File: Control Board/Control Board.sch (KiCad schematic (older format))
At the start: 77 parts, among them J1 Conn_02x03_Odd_Even, J2 Conn_02x25_Counter_Clockwise, Q1 STS4DNF60L, SW1 SW_SPDT, U1 ATXMEGA128A3-AU, U2 LT1797, U3 LT1797, U4 ISL83490, U5 MAX31856, U6 MAX31856, U7 MAX31856, U8 MAX31856, U9 MAX31856

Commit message: Updated power board to kicad 5
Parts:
- C1, C10, C11, C12, C13, C14, C15, C16, C17, C18, C19, C2, C20, C21, C22, C23, C24, C25, C26, C27, C28, C29, C3, C30, C31, C32, C33, C34, C35, C4, C5, C6, C7, C8, C9: symbol C_Small -> device:C_Small
- D1, D2, D3, D4: symbol LED -> device:LED
- J1: symbol Conn_02x03_Odd_Even -> Control-Board-rescue:Conn_02x03_Odd_Even
- J2: symbol Conn_02x25_Counter_Clockwise -> Control-Board-rescue:Conn_02x25_Counter_Clockwise
- L1: symbol L_Small -> device:L_Small
- Q1: symbol STS4DNF60L -> Custom-Parts:STS4DNF60L
- R1, R10, R11, R12, R13, R14, R15, R16, R17, R18, R19, R2, R20, R21, R3, R4, R5: symbol R_Small -> device:R_Small
- R22, R6, R7, R8, R9: symbol R -> device:R
- RN1, RN2: symbol Voltage_Divider_CenterPin3 -> device:Voltage_Divider_CenterPin3
- SW1: symbol SW_SPDT -> Control-Board-rescue:SW_SPDT
- U1: symbol ATXMEGA128A3-AU -> atmel:ATXMEGA128A3-AU
- U2, U3: symbol LT1797 -> Custom-Parts:LT1797
- U4: symbol ISL83490 -> Custom-Parts:ISL83490
- U5, U6, U7, U8, U9: symbol MAX31856 -> Custom-Parts:MAX31856
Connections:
- wire segments 235 -> 292

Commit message: Forgot an openlog on the control board
Had to get rid of the fault detect pins on the TCs, will have to poll for faults over SPI now
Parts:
- added U?: OPENLOG, symbol Custom-Parts:OPENLOG
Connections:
- net labels added: OPENLOG_RX, OPENLOG_TX
- net labels removed: BUZZER1, BUZZER2, TC1_FAULT, TC2_FAULT, TC3_FAULT, TC4_FAULT, TC5_FAULT
- wire segments 292 -> 288
- no-connect marks 0 -> 1

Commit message: A whole lot of changes
Kinda forgot what they all were
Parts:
- removed J2: Conn_02x25_Counter_Clockwise, Custom Footprints:CONN_CARD_02x25_MALE, symbol Control-Board-rescue:Conn_02x25_Counter_Clockwise
- removed R1, R2: 1.8 kΩ, Resistors_SMD:R_0603, symbol device:R_Small
- added J1: Conn_02x10_Odd_Even, symbol Connector:Conn_02x10_Odd_Even
- added J?: RJ45, Connectors:RJ45_8, symbol Connector:RJ45
- added J? (x4): GS3, Connectors:GS3, symbol Connector:GS3
- added J?: Conn_01x10, Connectors_JST:JST_PH_S10B-PH-K_10x2.00mm_Angled, symbol Connector:Conn_01x10
- renumbered J1 to J2
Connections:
- net labels removed: +14V
- wire segments 288 -> 305
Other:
- note removed: "Close to power supply"
- note removed: "TODO: Figure out how to control the servos\nThis assumes its 5V PWM, change this if it's not"
- moved on the sheet: R3, R4

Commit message: Starting to make control board match power board
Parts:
- removed J? (x4): GS3, Connectors:GS3, symbol Connector:GS3
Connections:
- wire segments 305 -> 285
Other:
- note added: "Needs crossover cable"
- moved on the sheet: J?
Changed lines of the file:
@@
 L power:+3V3 #PWR075
 U 1 1 5A835285
-P 13800 11300
-F 0 "#PWR075" H 13800 11150 50  0001 C CNN
-F 1 "+3V3" V 13800 11500 50  0000 C CNN
-F 2 "" H 13800 11300 50  0001 C CNN
-F 3 "" H 13800 11300 50  0001 C CNN
-	1    13800 11300
+P 14350 10750
+F 0 "#PWR075" H 14350 10600 50  0001 C CNN
+F 1 "+3V3" V 14350 10950 50  0000 C CNN
+F 2 "" H 14350 10750 50  0001 C CNN
+F 3 "" H 14350 10750 50  0001 C CNN
+	1    14350 10750
 	0    -1   -1   0
 $EndComp
@@
 Text Label 2150 4600 2    60   ~ 0
 BOARD_TX
-Text Label 12600 13100 3    60   ~ 0
+Text Label 12000 12650 3    60   ~ 0
 BOARD_RX+
-Text Label 11800 13100 3    60   ~ 0
+Text Label 11800 12650 3    60   ~ 0
 BOARD_TX+
-Text Label 13000 13100 3    60   ~ 0
+Text Label 12300 12650 3    60   ~ 0
 BOARD_RX-
-Text Label 12200 13100 3    60   ~ 0
+Text Label 11900 12650 3    60   ~ 0
 BOARD_TX-
 Text Label 8450 12250 2    60   ~ 0
@@
 L power:GND #PWR092
 U 1 1 5A9DF128
-P 13700 11900
-F 0 "#PWR092" H 13700 11650 50  0001 C CNN
-F 1 "GND" V 13700 11700 50  0000 C CNN
-F 2 "" H 13700 11900 50  0001 C CNN
-F 3 "" H 13700 11900 50  0001 C CNN
-	1    13700 11900
-	0    -1   1    0
+P 14350 10850
+F 0 "#PWR092" H 14350 10600 50  0001 C CNN
+F 1 "GND" V 14350 10650 50  0000 C CNN
+F 2 "" H 14350 10850 50  0001 C CNN
+F 3 "" H 14350 10850 50  0001 C CNN
+	1    14350 10850
+	0    1    -1   0
 $EndComp
 Text Label 14350 12250 2    60   ~ 0
@@
 L power:GND #PWR?
 U 1 1 5AB3D167
-P 12700 11500
-F 0 "#PWR?" H 12700 11250 50  0001 C CNN
-F 1 "GND" V 12700 11300 50  0000 C CNN
-F 2 "" H 12700 11500 50  0001 C CNN
-F 3 "" H 12700 11500 50  0001 C CNN
-	1    12700 11500
+P 12700 11850
+F 0 "#PWR?" H 12700 11600 50  0001 C CNN
+F 1 "GND" V 12700 11650 50  0000 C CNN
+F 2 "" H 12700 11850 50  0001 C CNN
+F 3 "" H 12700 11850 50  0001 C CNN
+	1    12700 11850
 	0    -1   1    0
 $EndComp
@@
 L Connector:RJ45 J?
 U 1 1 5ADD31C9
-P 12150 11850
-F 0 "J?" H 12226 12467 50  0000 C CNN
-F 1 "RJ45" H 12226 12376 50  0000 C CNN
-F 2 "Connectors:RJ45_8" H 12150 11850 50  0001 C CNN
-F 3 "" H 12150 11850 50  0001 C CNN
-	1    12150 11850
+P 12150 12200
+F 0 "J?" H 12226 12817 50  0000 C CNN
+F 1 "RJ45" H 12226 12726 50  0000 C CNN
+F 2 "Connectors:RJ45_8" H 12150 12200 50  0001 C CNN
+F 3 "" H 12150 12200 50  0001 C CNN
+	1    12150 12200
 	1    0    0    -1
 $EndComp
-$Comp
-L Connector:GS3 J?
-U 1 1 5AE56887
-P 11800 12950
-F 0 "J?" V 11754 13118 50  0000 L CNN
-F 1 "GS3" V 11845 13118 50  0000 L CNN
-F 2 "Connectors:GS3" V 11888 12876 50  0001 C CNN
-F 3 "" H 11800 12950 50  0001 C CNN
-	1    11800 12950
-	0    1    1    0
-$EndComp
-$Comp
-L Connector:GS3 J?
-U 1 1 5AE74912
-P 12200 12950
-F 0 "J?" V 12154 13118 50  0000 L CNN
-F 1 "GS3" V 12245 13118 50  0000 L CNN
-F 2 "Connectors:GS3" V 12288 12876 50  0001 C CNN
-F 3 "" H 12200 12950 50  0001 C CNN
-	1    12200 12950
-	0    1    1    0
-$EndComp
-$Comp
-L Connector:GS3 J?
-U 1 1 5AE74AB9
-P 12600 12950
-F 0 "J?" V 12554 13118 50  0000 L CNN
-F 1 "GS3" V 12645 13118 50  0000 L CNN
-F 2 "Connectors:GS3" V 12688 12876 50  0001 C CNN
-F 3 "" H 12600 12950 50  0001 C CNN
-	1    12600 12950
-	0    1    1    0
-$EndComp
-$Comp
-L Connector:GS3 J?
-U 1 1 5AE74C5F
-P 13000 12950
-F 0 "J?" V 12954 13118 50  0000 L CNN
-F 1 "GS3" V 13045 13118 50  0000 L CNN
-F 2 "Connectors:GS3" V 13088 12876 50  0001 C CNN
-F 3 "" H 13000 12950 50  0001 C CNN
-	1    13000 12950
-	0    1    1    0
-$EndComp
-Wire Wire Line
-	11900 12800 11900 12700
-Wire Wire Line
-	11900 12700 11800 12700
-Wire Wire Line
-	11800 12700 11800 12300
-Wire Wire Line
-	12300 12800 12300 12600
-Wire Wire Line
-	12300 12600 11900 12600
-Wire Wire Line
-	11900 12600 11900 12300
-Wire Wire Line
-	12700 12800 12700 12500
-Wire Wire Line
-	12700 12500 12000 12500
-Wire Wire Line
-	12000 12500 12000 12300
-Wire Wire Line
-	13100 12800 13100 12400
-Wire Wire Line
-	13100 12400 12300 12400
-Wire Wire Line
-	12300 12400 12300 12300
-Wire Wire Line
-	11700 12800 11700 12500
-Wire Wire Line
-	11700 12500 12000 12500
-Connection ~ 12000 12500
-Wire Wire Line
-	12100 12800 12100 12400
-Wire Wire Line
-	12100 12400 12300 12400
-Connection ~ 12300 12400
-Wire Wire Line
-	12500 12800 12500 12700
-Wire Wire Line
-	12500 12700 11900 12700
-Connection ~ 11900 12700
-Wire Wire Line
-	12900 12800 12900 12600
-Wire Wire Line
-	12900 12600 12300 12600
-Connection ~ 12300 12600
 $Comp
 L Connector:Conn_01x10 J?
@@
 	1    0    0    -1
 $EndComp
+Text Notes 11750 11550 0    50   ~ 0
+Needs crossover cable
 $EndSCHEMATC

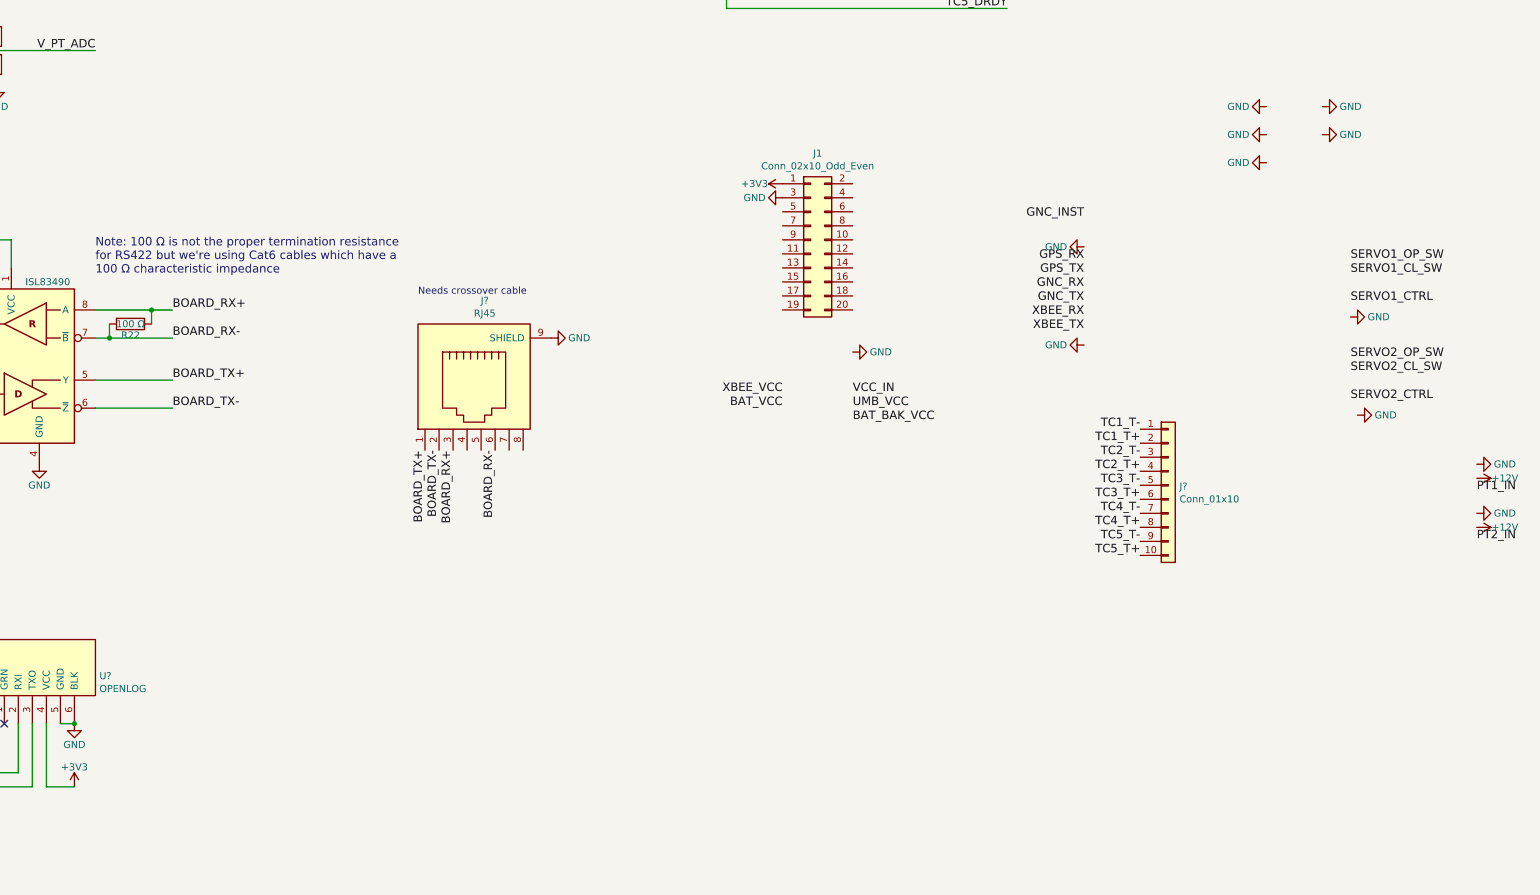
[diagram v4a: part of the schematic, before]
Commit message: Updated control board schematic
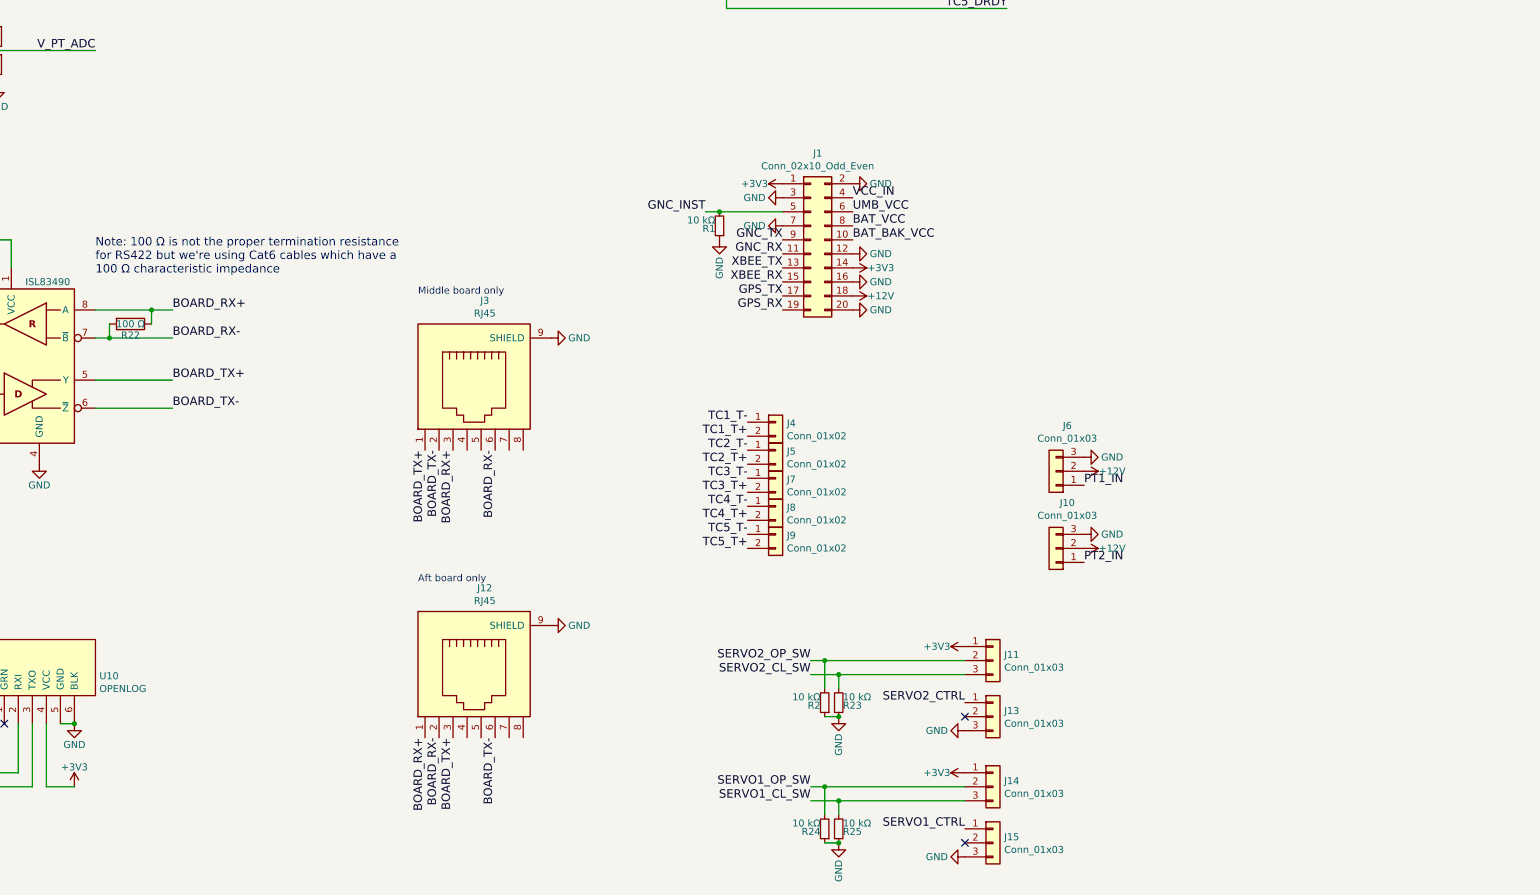
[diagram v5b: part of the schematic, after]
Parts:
- removed J?: Conn_01x10, Connectors_JST:JST_PH_S10B-PH-K_10x2.00mm_Angled, symbol Connector:Conn_01x10
- added J10, J11, J13, J14, J15, J6: Conn_01x03, symbol Connector:Conn_01x03
- added J12: RJ45, Connectors:RJ45_8, symbol Connector:RJ45
- added J4, J5, J7, J8, J9: Conn_01x02, symbol Connector:Conn_01x02
- added R1, R2, R23, R24, R25: 10 kΩ, Resistors_SMD:R_0603, symbol device:R_Small
- J1: footprint (none) -> Pin_Headers:Pin_Header_Straight_2x10_Pitch1.27mm
- gave numbers to parts that had none: 2
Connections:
- net +12V: now also J1.18 (Pin_18), J10.2 (Pin_2), J6.2 (Pin_2)
- net +3V3: now also J1.14 (Pin_14), J11.1 (Pin_1), J14.1 (Pin_1)
- net BAT_BAK_VCC: now also J1.10 (Pin_10)
- net BAT_VCC: now also J1.8 (Pin_8)
- net BOARD_RX+: now also J12.1
- net BOARD_RX-: now also J12.2
- net BOARD_TX+: now also J12.3
- net BOARD_TX-: now also J12.6
- net GNC_INST: now also J1.5 (Pin_5), R1.2
- net GNC_RX: now also J1.11 (Pin_11)
- net GNC_TX: now also J1.9 (Pin_9)
- net GND: now also J1.12 (Pin_12), J1.16 (Pin_16), J1.2 (Pin_2), J1.20 (Pin_20), J1.7 (Pin_7), J10.3 (Pin_3), J12.9 (SHIELD), J13.3 (Pin_3), J15.3 (Pin_3), J6.3 (Pin_3), R1.1, R2.1, R23.1, R24.1, R25.1
- net GPS_RX: now also J1.19 (Pin_19)
- net GPS_TX: now also J1.17 (Pin_17)
- net PT1_IN: now also J6.1 (Pin_1)
- net PT2_IN: now also J10.1 (Pin_1)
- net SERVO1_CL_SW: now also J14.3 (Pin_3), R25.2
- net SERVO1_CTRL: now also J15.1 (Pin_1)
- net SERVO1_OP_SW: now also J14.2 (Pin_2), R24.2
- net SERVO2_CL_SW: now also J11.3 (Pin_3), R23.2
- net SERVO2_CTRL: now also J13.1 (Pin_1)
- net SERVO2_OP_SW: now also J11.2 (Pin_2), R2.2
- net TC1_T+: now also J4.2 (Pin_2)
- net TC1_T-: now also J4.1 (Pin_1)
- net TC2_T+: now also J5.2 (Pin_2)
- net TC2_T-: now also J5.1 (Pin_1)
- net TC3_T+: now also J7.2 (Pin_2)
- net TC3_T-: now also J7.1 (Pin_1)
- net TC4_T+: now also J8.2 (Pin_2)
- net TC4_T-: now also J8.1 (Pin_1)
- net TC5_T+: now also J9.2 (Pin_2)
- net TC5_T-: now also J9.1 (Pin_1)
- net UMB_VCC: now also J1.6 (Pin_6)
- net VCC_IN: now also J1.4 (Pin_4)
- net XBEE_RX: now also J1.15 (Pin_15)
- net XBEE_TX: now also J1.13 (Pin_13)
- no-connect marks 1 -> 3
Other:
- note added: "Aft board only"
- note added: "Middle board only"
- note removed: "Needs crossover cable"

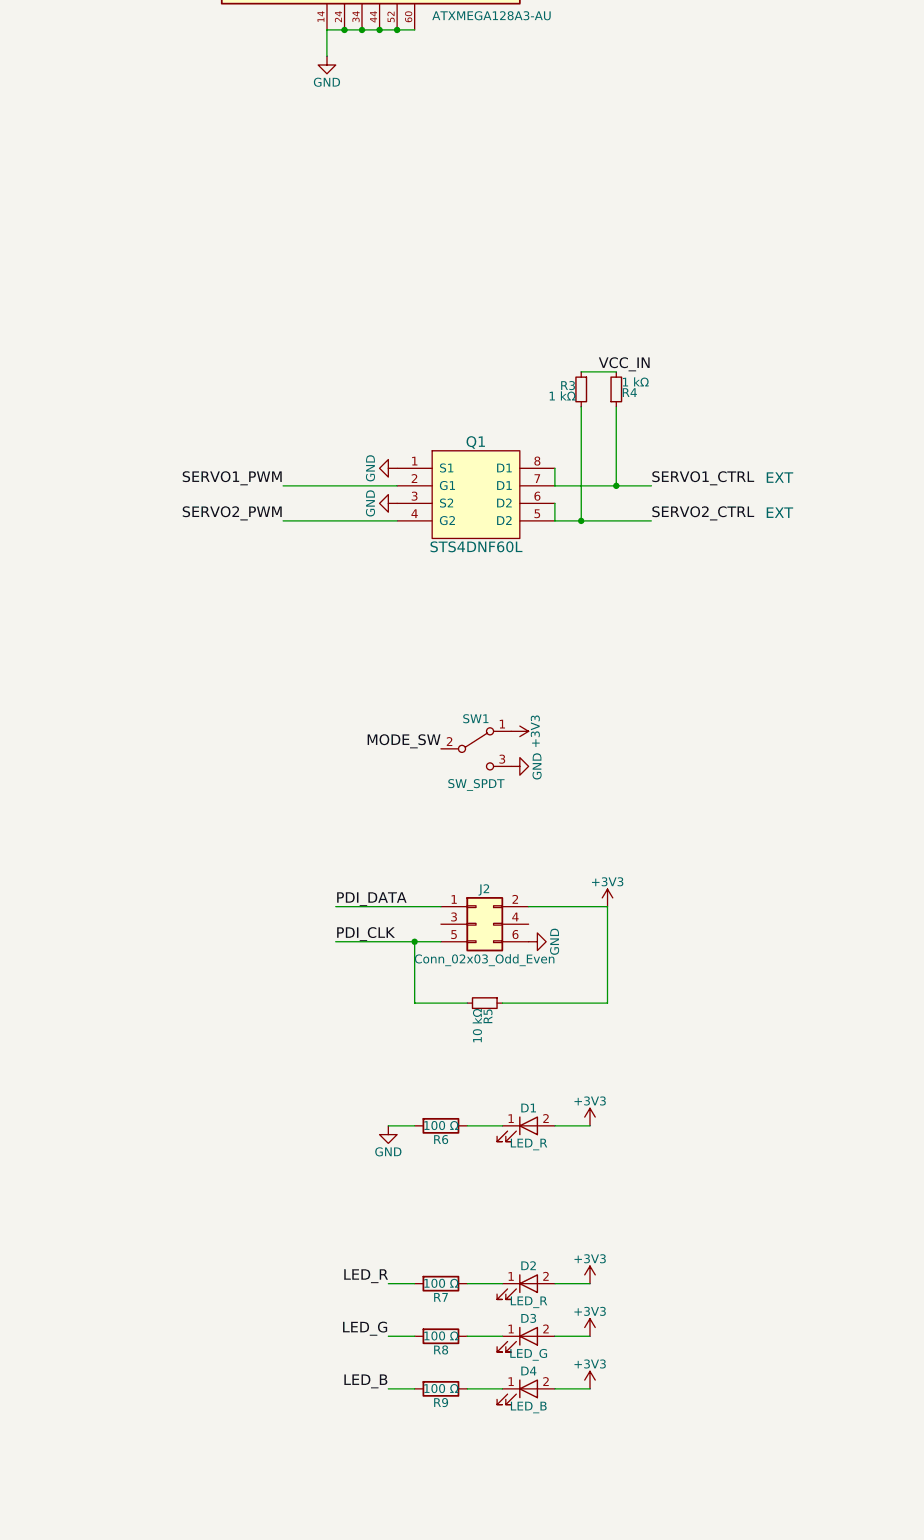
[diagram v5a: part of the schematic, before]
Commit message: Added footprints to new stuff on control board
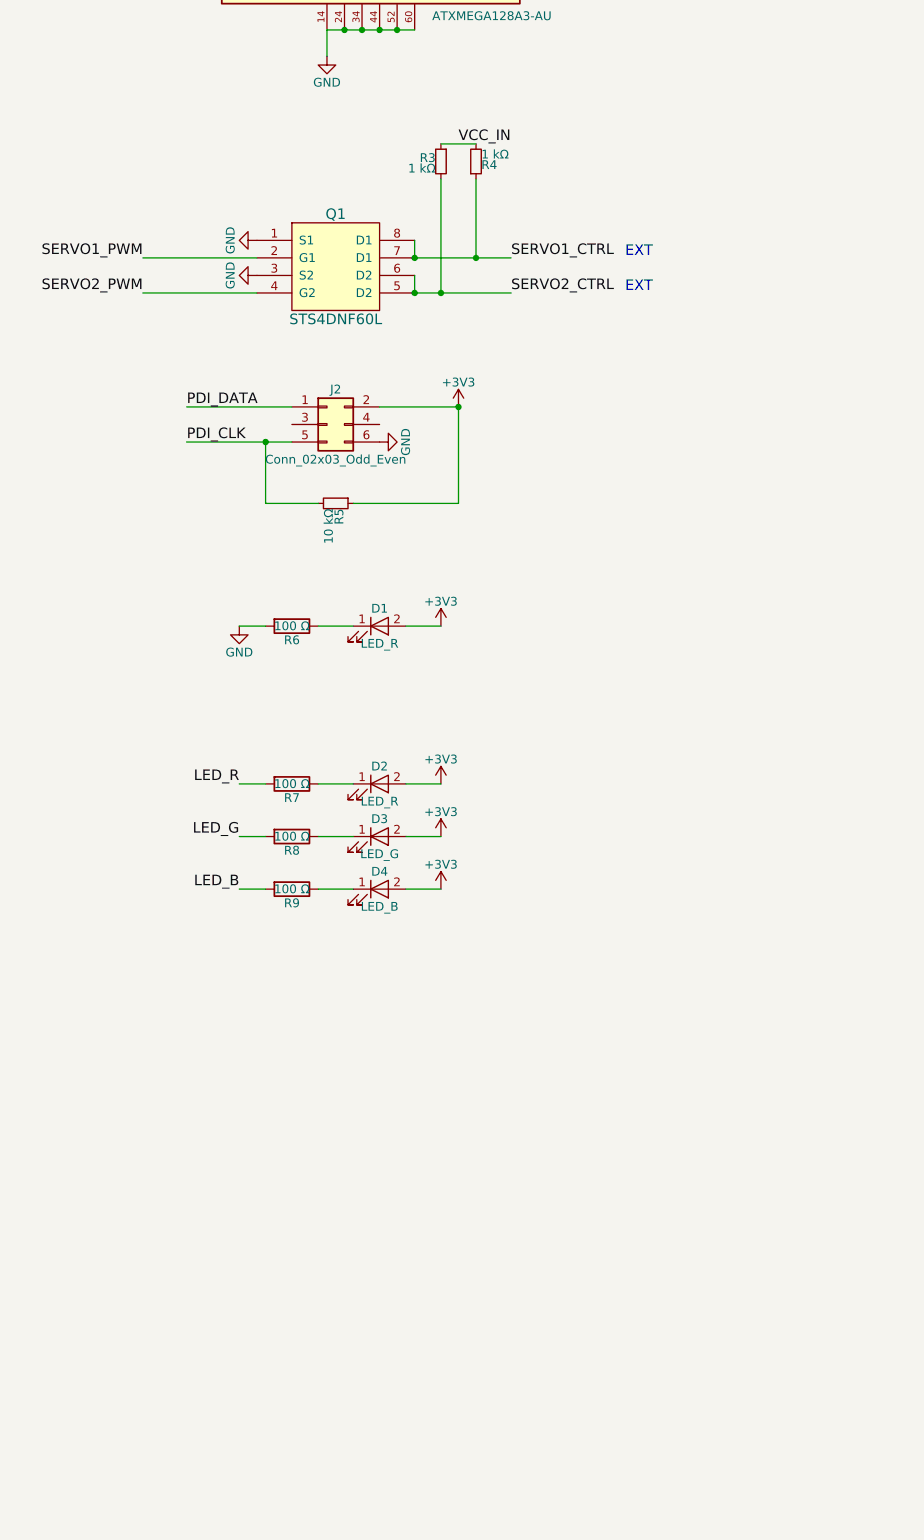
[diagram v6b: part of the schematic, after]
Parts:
- removed SW1: SW_SPDT, Buttons_Switches_SMD:SW_SPDT_CK-JS102011SAQN, symbol Control-Board-rescue:SW_SPDT
- J10, J11, J13, J14, J15: footprint (none) -> Connectors_JST:JST_PH_S3B-PH-K_03x2.00mm_Angled
- J4, J5, J6, J7, J8, J9: footprint (none) -> Connectors_JST:JST_PH_S2B-PH-K_02x2.00mm_Angled
- U10: footprint (none) -> Custom Footprints:OpenLog
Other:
- moved on the sheet: D1, D2, D3, D4, J2, Q1, R3, R4, R5, R6, R7, R8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
